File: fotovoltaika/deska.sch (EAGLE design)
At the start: 19 parts

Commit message: upravy desek
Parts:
- removed R1, R11, R2, R3, R4, R5, R6, R7, R8, R9: (no value), rcl:R-EU_0207/7
- removed X1, X2, X3, X4: (no value), con-wago-508:W237-02P
- added SL3, SL4: (no value), con-amp-quick:M04
- added SUPPLY: (no value), con-wago-508:W237-02P
- SL1: device con-amp-quick:M10 -> con-amp-quick:M04
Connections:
- removed net N$10: R4.2, X4-1.KL
- removed net N$13: R11.2, R9.1, WEMOS1.D7
- removed net N$3: R1.2, X1-1.KL
- removed net N$4: R1.1, R5.2, SL1.1
- removed net N$5: R2.1, R6.2, SL1.2
- removed net N$6: R3.1, R7.2, SL1.3
- removed net N$7: R4.1, R8.2, SL1.4
- removed net N$8: R2.2, X2-1.KL
- removed net N$9: R3.2, X3-1.KL
- net +5V: now also SL1.1, SL3.1, SL4.1, SUPPLY-2.KL; no longer SL1.10
- net GND: now also SL1.2, SL3.2, SL4.2, SUPPLY-1.KL; no longer R11.1, R5.1, R6.1, R7.1, R8.1, SL1.6, SL1.9, X1-2.KL, X2-2.KL, X3-2.KL, X4-2.KL
- net N$1: now also SL1.4, SL2.4, SL3.4, SL4.4, WEMOS1.D1; no longer SL1.7, WEMOS1.D2
- net N$2: now also SL1.3, SL2.3, SL3.3, SL4.3, WEMOS1.D2; no longer SL1.8, WEMOS1.D1
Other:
- moved on the sheet: SL2

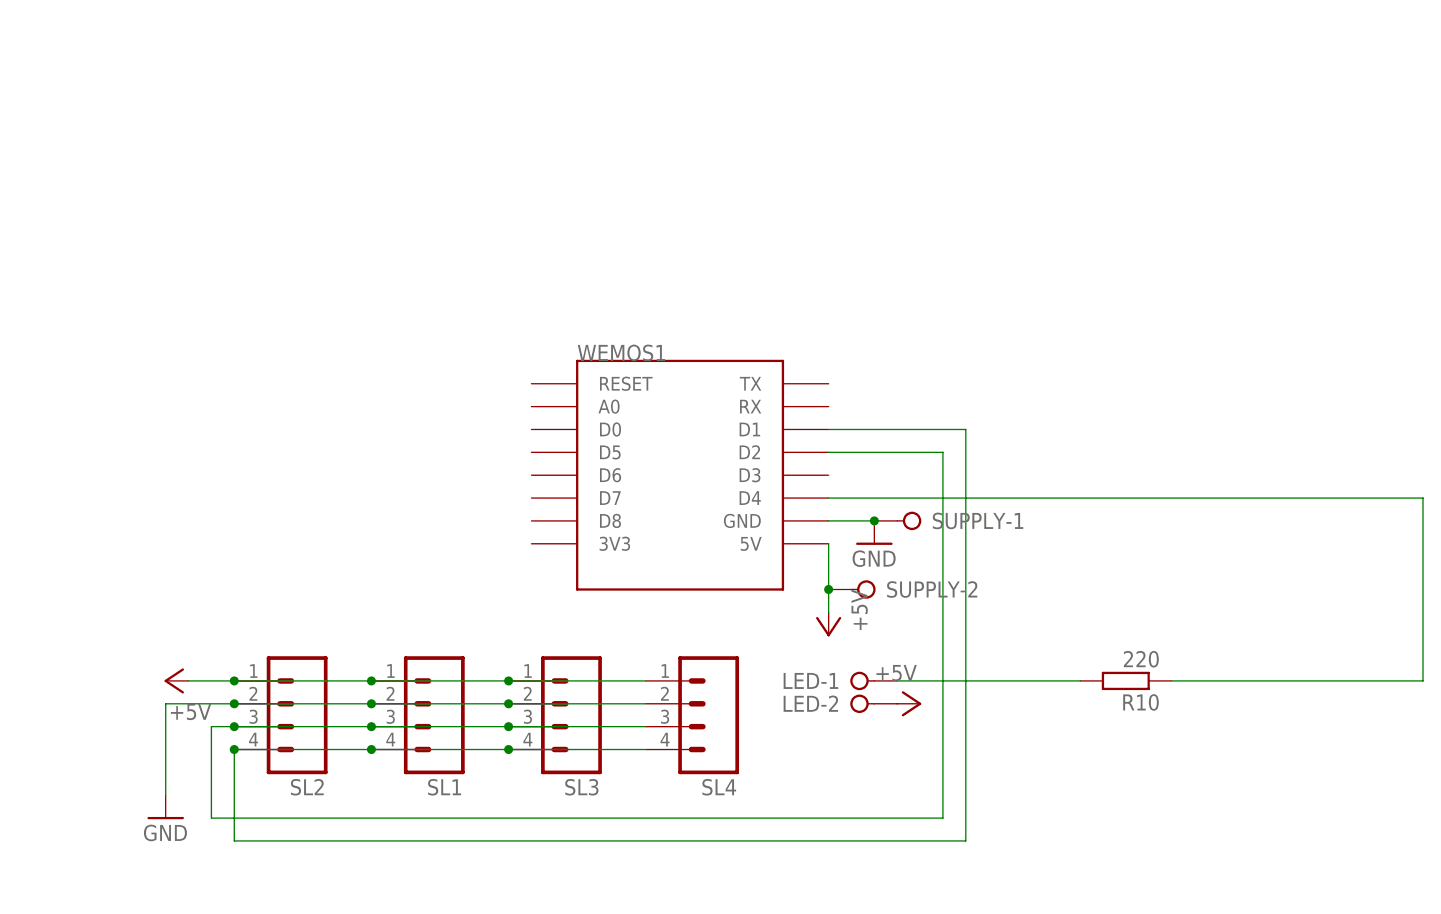
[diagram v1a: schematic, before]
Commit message: uprava desky ovladani rele
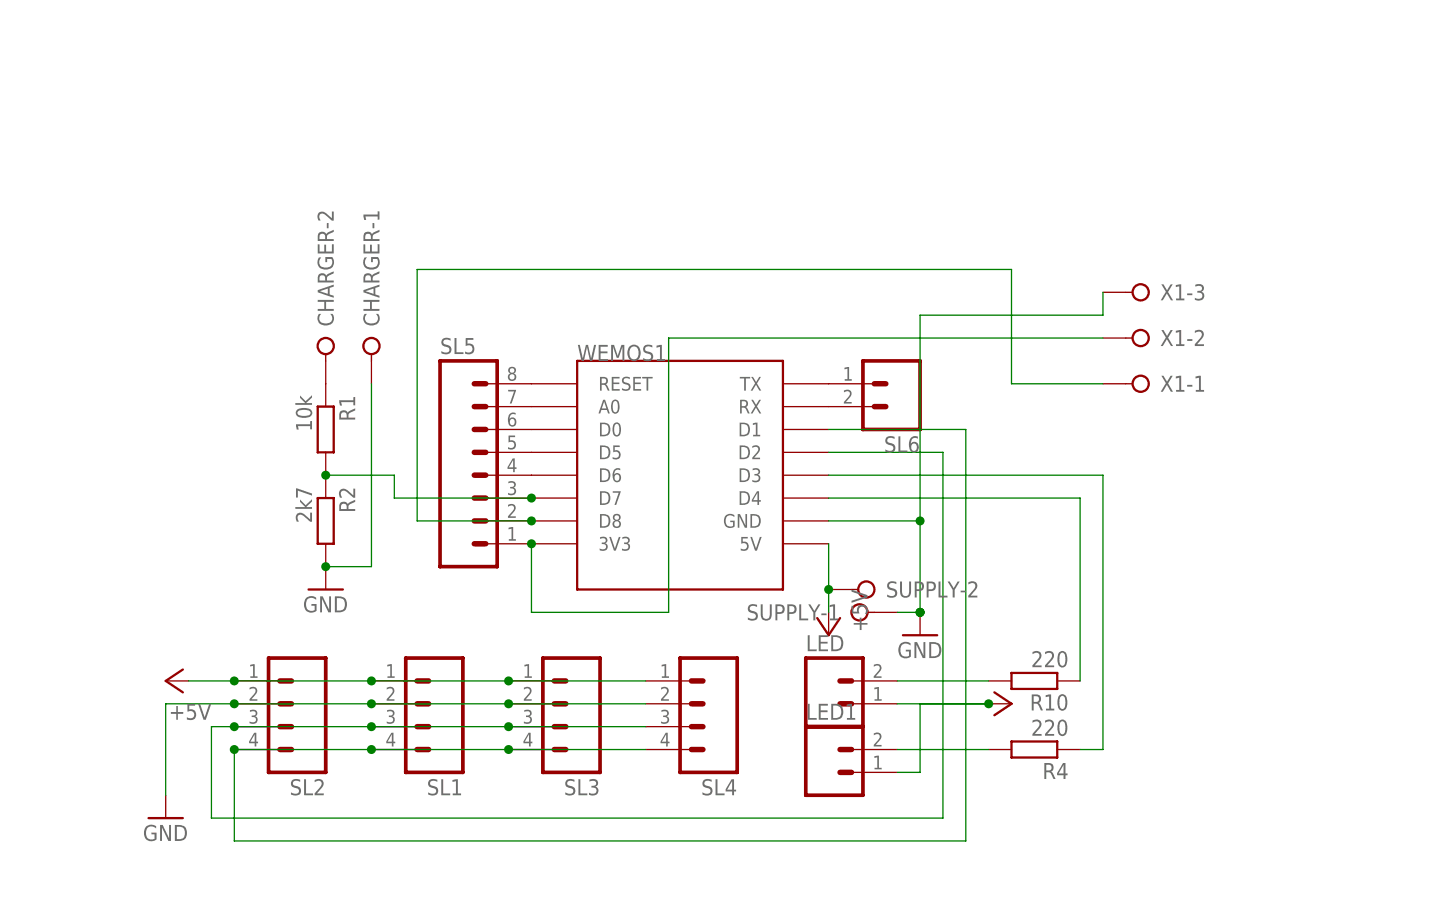
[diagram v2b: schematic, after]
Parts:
- added CHARGER: (no value), con-wago-508:W237-02P
- added LED1, SL6: (no value), con-amp-quick:M02
- added R1: 10k, rcl:R-EU_0207/10
- added R2: 2k7, rcl:R-EU_0207/10
- added R4: 220, rcl:R-EU_0207/10
- added SL5: (no value), con-amp-quick:M08
- added X1: (no value), con-wago-508:W237-3E
- LED: device con-wago-508:W237-02P -> con-amp-quick:M02
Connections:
- new net N$10: R1.2, R2.1, SL5.3, WEMOS1.D7
- new net N$13: SL5.8, WEMOS1.RESET
- new net N$14: SL6.1, WEMOS1.TX
- new net N$15: SL6.2, WEMOS1.RX
- new net N$16: LED1.2, R4.2
- new net N$17: R4.1, WEMOS1.D3
- new net N$18: SL5.1, WEMOS1.3V3, X1-2.KL
- new net N$3: SL5.7, WEMOS1.A0
- new net N$4: SL5.2, WEMOS1.D8, X1-1.KL
- new net N$5: CHARGER-2.KL, R1.1
- new net N$7: SL5.4, WEMOS1.D6
- new net N$8: SL5.5, WEMOS1.D5
- new net N$9: SL5.6, WEMOS1.D0
- net +5V: now also LED.1, LED1.1; no longer LED-2.KL
- net GND: now also CHARGER-1.KL, R2.2, X1-3.KL
- net N$12: now also LED.2; no longer LED-1.KL
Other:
- moved on the sheet: R10, SUPPLY-1

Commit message: uprava desky
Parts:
- removed SL6: (no value), con-amp-quick:M02
- removed X1: (no value), con-wago-508:W237-3E
- added MODEM: (no value), con-amp-quick:M02
- added RELAY: (no value), con-wago-508:W237-3E
- renumbered SL1 to INA219, SL2 to DISPLAY
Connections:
- removed net N$18: SL5.1, WEMOS1.3V3, X1-2.KL
- new net +3V3: RELAY-2.KL, SL5.1, WEMOS1.3V3
- net GND: now also RELAY-3.KL; no longer X1-3.KL
- net N$14: now also MODEM.1; no longer SL6.1
- net N$15: now also MODEM.2; no longer SL6.2
- net N$4: now also RELAY-1.KL; no longer X1-1.KL
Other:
- moved on the sheet: SUPPLY-1

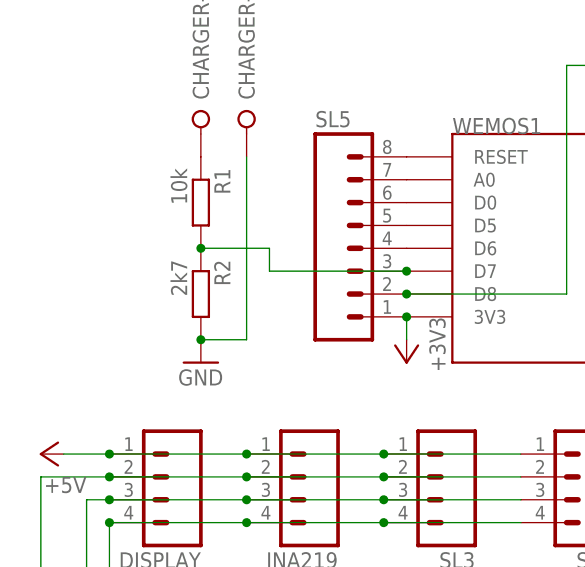
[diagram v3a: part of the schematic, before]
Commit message: zmena odporu delice
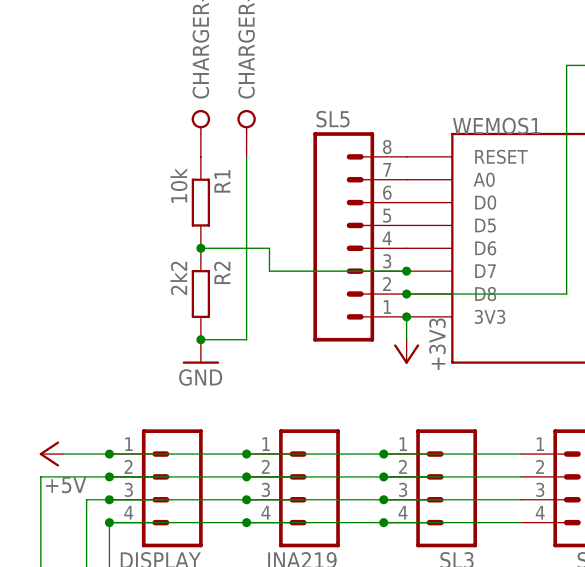
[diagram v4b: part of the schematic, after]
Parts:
- R2: value 2k7 -> 2k2
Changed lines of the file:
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@@
 <?xml version="1.0" encoding="utf-8"?>
 <!DOCTYPE eagle SYSTEM "eagle.dtd">
-<eagle version="9.4.1">
+<eagle version="9.3.0">
 <drawing>
 <settings>
@@
 <part name="SL4" library="con-amp-quick" library_urn="urn:adsk.eagle:library:125" deviceset="M04" device="" package3d_urn="urn:adsk.eagle:package:5958/1"/>
 <part name="SUPPLY" library="con-wago-508" deviceset="W237-02P" device=""/>
-<part name="R1" library="rcl" deviceset="R-EU_" device="0207/10" override_package3d_urn="urn:adsk.eagle:package:11209799/2" override_package_urn="urn:adsk.eagle:footprint:11209800/1" value="10k"/>
-<part name="R2" library="rcl" deviceset="R-EU_" device="0207/10" override_package3d_urn="urn:adsk.eagle:package:11209793/2" override_package_urn="urn:adsk.eagle:footprint:11209794/1" value="2k7"/>
+<part name="R1" library="rcl" deviceset="R-EU_" device="0207/10" value="10k"/>
+<part name="R2" library="rcl" deviceset="R-EU_" device="0207/10" value="2k2"/>
 <part name="GND1" library="supply1" deviceset="GND" device=""/>
 <part name="CHARGER" library="con-wago-508" deviceset="W237-02P" device=""/>
@@
 packages will not be understood (or retained) with this version.
 </note>
-<note version="9.4" severity="warning">
-Since Version 9.4, EAGLE supports the overriding of 3D packages
-in schematics and board files. Those overridden 3d packages
-will not be understood (or retained) with this version.
-</note>
 </compatibility>
